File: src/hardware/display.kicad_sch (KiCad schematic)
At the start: 6 parts, among them J1 046809612110846+, U6 TXS0108ERKSR, U7 LP5817YCHR

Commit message: Add Light Sensor and Proximity & Gesture Sensor; Changed GPIO
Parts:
- renumbered R22 to R23
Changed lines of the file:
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@@
 		(dnp no)
 		(fields_autoplaced yes)
-		(property "Reference" "#PWR079"
+		(property "Reference" "#PWR080"
 			(at 90.17 130.81 0)
 			(effects
@@
 			(project "raywatch"
 				(path "/7b654ee8-2a53-4d39-8b7d-32c7bb3cb0ed/0522506d-d6b7-4115-aecc-a1b886294452"
-					(reference "#PWR079")
+					(reference "#PWR080")
 					(unit 1)
 				)
@@
 		(dnp no)
 		(fields_autoplaced yes)
-		(property "Reference" "#PWR094"
+		(property "Reference" "#PWR095"
 			(at 215.9 69.85 0)
 			(effects
@@
 			(project "raywatch"
 				(path "/7b654ee8-2a53-4d39-8b7d-32c7bb3cb0ed/0522506d-d6b7-4115-aecc-a1b886294452"
-					(reference "#PWR094")
+					(reference "#PWR095")
 					(unit 1)
 				)
@@
 		(dnp no)
 		(fields_autoplaced yes)
-		(property "Reference" "#PWR082"
+		(property "Reference" "#PWR083"
 			(at 110.49 40.64 0)
 			(effects
@@
 			(project "raywatch"
 				(path "/7b654ee8-2a53-4d39-8b7d-32c7bb3cb0ed/0522506d-d6b7-4115-aecc-a1b886294452"
-					(reference "#PWR082")
+					(reference "#PWR083")
 					(unit 1)
 				)
@@
 		(dnp no)
 		(fields_autoplaced yes)
-		(property "Reference" "R22"
+		(property "Reference" "R23"
 			(at 102.87 63.5 90)
 			(effects
@@
 			(project "raywatch"
 				(path "/7b654ee8-2a53-4d39-8b7d-32c7bb3cb0ed/0522506d-d6b7-4115-aecc-a1b886294452"
-					(reference "R22")
+					(reference "R23")
 					(unit 1)
 				)
@@
 		(dnp no)
 		(fields_autoplaced yes)
-		(property "Reference" "#PWR080"
+		(property "Reference" "#PWR081"
 			(at 90.17 140.97 0)
 			(effects
@@
 			(project "raywatch"
 				(path "/7b654ee8-2a53-4d39-8b7d-32c7bb3cb0ed/0522506d-d6b7-4115-aecc-a1b886294452"
-					(reference "#PWR080")
+					(reference "#PWR081")
 					(unit 1)
 				)
@@
 		(dnp no)
 		(fields_autoplaced yes)
-		(property "Reference" "#PWR087"
+		(property "Reference" "#PWR088"
 			(at 106.68 138.43 0)
 			(effects
@@
 			(project "raywatch"
 				(path "/7b654ee8-2a53-4d39-8b7d-32c7bb3cb0ed/0522506d-d6b7-4115-aecc-a1b886294452"
-					(reference "#PWR087")
+					(reference "#PWR088")
 					(unit 1)
 				)
@@
 		(dnp no)
 		(fields_autoplaced yes)
-		(property "Reference" "#PWR090"
+		(property "Reference" "#PWR091"
 			(at 176.53 87.63 0)
 			(effects
@@
 			(project "raywatch"
 				(path "/7b654ee8-2a53-4d39-8b7d-32c7bb3cb0ed/0522506d-d6b7-4115-aecc-a1b886294452"
-					(reference "#PWR090")
+					(reference "#PWR091")
 					(unit 1)
 				)
@@
 		(dnp no)
 		(fields_autoplaced yes)
-		(property "Reference" "#PWR088"
+		(property "Reference" "#PWR089"
 			(at 153.67 114.3 0)
 			(effects
@@
 			(project "raywatch"
 				(path "/7b654ee8-2a53-4d39-8b7d-32c7bb3cb0ed/0522506d-d6b7-4115-aecc-a1b886294452"
-					(reference "#PWR088")
+					(reference "#PWR089")
 					(unit 1)
 				)
@@
 		(dnp no)
 		(fields_autoplaced yes)
-		(property "Reference" "#PWR083"
+		(property "Reference" "#PWR084"
 			(at 110.49 43.18 0)
 			(effects
@@
 			(project "raywatch"
 				(path "/7b654ee8-2a53-4d39-8b7d-32c7bb3cb0ed/0522506d-d6b7-4115-aecc-a1b886294452"
-					(reference "#PWR083")
+					(reference "#PWR084")
 					(unit 1)
 				)
@@
 		(dnp no)
 		(fields_autoplaced yes)
-		(property "Reference" "#PWR084"
+		(property "Reference" "#PWR085"
 			(at 100.33 48.26 0)
 			(effects
@@
 			(project "raywatch"
 				(path "/7b654ee8-2a53-4d39-8b7d-32c7bb3cb0ed/0522506d-d6b7-4115-aecc-a1b886294452"
-					(reference "#PWR084")
+					(reference "#PWR085")
 					(unit 1)
 				)
@@
 		(dnp no)
 		(fields_autoplaced yes)
-		(property "Reference" "#PWR089"
+		(property "Reference" "#PWR090"
 			(at 165.1 93.98 0)
 			(effects
@@
 			(project "raywatch"
 				(path "/7b654ee8-2a53-4d39-8b7d-32c7bb3cb0ed/0522506d-d6b7-4115-aecc-a1b886294452"
-					(reference "#PWR089")
+					(reference "#PWR090")
 					(unit 1)
 				)
@@
 		(dnp no)
 		(fields_autoplaced yes)
-		(property "Reference" "#PWR081"
+		(property "Reference" "#PWR082"
 			(at 92.71 69.85 0)
 			(effects
@@
 			(project "raywatch"
 				(path "/7b654ee8-2a53-4d39-8b7d-32c7bb3cb0ed/0522506d-d6b7-4115-aecc-a1b886294452"
-					(reference "#PWR081")
+					(reference "#PWR082")
 					(unit 1)
 				)
@@
 		(dnp no)
 		(fields_autoplaced yes)
-		(property "Reference" "#PWR085"
+		(property "Reference" "#PWR086"
 			(at 100.33 50.8 0)
 			(effects
@@
 			(project "raywatch"
 				(path "/7b654ee8-2a53-4d39-8b7d-32c7bb3cb0ed/0522506d-d6b7-4115-aecc-a1b886294452"
-					(reference "#PWR085")
+					(reference "#PWR086")
 					(unit 1)
 				)
@@
 		(dnp no)
 		(fields_autoplaced yes)
-		(property "Reference" "#PWR091"
+		(property "Reference" "#PWR092"
 			(at 166.37 90.17 0)
 			(effects
@@
 			(project "raywatch"
 				(path "/7b654ee8-2a53-4d39-8b7d-32c7bb3cb0ed/0522506d-d6b7-4115-aecc-a1b886294452"
-					(reference "#PWR091")
+					(reference "#PWR092")
 					(unit 1)
 				)
@@
 		(dnp no)
 		(fields_autoplaced yes)
-		(property "Reference" "#PWR095"
+		(property "Reference" "#PWR096"
 			(at 215.9 72.39 0)
 			(effects
@@
 			(project "raywatch"
 				(path "/7b654ee8-2a53-4d39-8b7d-32c7bb3cb0ed/0522506d-d6b7-4115-aecc-a1b886294452"
-					(reference "#PWR095")
+					(reference "#PWR096")
 					(unit 1)
 				)
@@
 		(dnp no)
 		(fields_autoplaced yes)
-		(property "Reference" "#PWR086"
+		(property "Reference" "#PWR087"
 			(at 100.33 121.92 0)
 			(effects
@@
 			(project "raywatch"
 				(path "/7b654ee8-2a53-4d39-8b7d-32c7bb3cb0ed/0522506d-d6b7-4115-aecc-a1b886294452"
-					(reference "#PWR086")
+					(reference "#PWR087")
 					(unit 1)
 				)
@@
 		(dnp no)
 		(fields_autoplaced yes)
-		(property "Reference" "#PWR093"
+		(property "Reference" "#PWR094"
 			(at 173.99 63.5 0)
 			(effects
@@
 			(project "raywatch"
 				(path "/7b654ee8-2a53-4d39-8b7d-32c7bb3cb0ed/0522506d-d6b7-4115-aecc-a1b886294452"
-					(reference "#PWR093")
+					(reference "#PWR094")
 					(unit 1)
 				)
@@
 		(dnp no)
 		(fields_autoplaced yes)
-		(property "Reference" "#PWR092"
+		(property "Reference" "#PWR093"
 			(at 172.72 111.76 0)
 			(effects
@@
 			(project "raywatch"
 				(path "/7b654ee8-2a53-4d39-8b7d-32c7bb3cb0ed/0522506d-d6b7-4115-aecc-a1b886294452"
-					(reference "#PWR092")
-					(unit 1)
-				)
+					(reference "#PWR093")
+					(unit 1)
+				)

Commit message: Changed footprints from 0603 to 0402
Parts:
- C28, C29: footprint Capacitor_SMD:C_0603_1608Metric -> Capacitor_SMD:C_0504_1310Metric
- R23: footprint Resistor_SMD:R_0603_1608Metric -> Resistor_SMD:R_0402_1005Metric
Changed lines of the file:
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@@
 			)
 		)
-		(property "Footprint" "Resistor_SMD:R_0603_1608Metric"
+		(property "Footprint" "Resistor_SMD:R_0402_1005Metric"
 			(at 102.87 71.628 90)
 			(effects
@@
 			)
 		)
-		(property "Footprint" "Capacitor_SMD:C_0603_1608Metric"
+		(property "Footprint" "Capacitor_SMD:C_0504_1310Metric"
 			(at 173.6852 105.41 0)
 			(effects
@@
 			)
 		)
-		(property "Footprint" "Capacitor_SMD:C_0603_1608Metric"
+		(property "Footprint" "Capacitor_SMD:C_0504_1310Metric"
 			(at 91.1352 134.62 0)
 			(effects

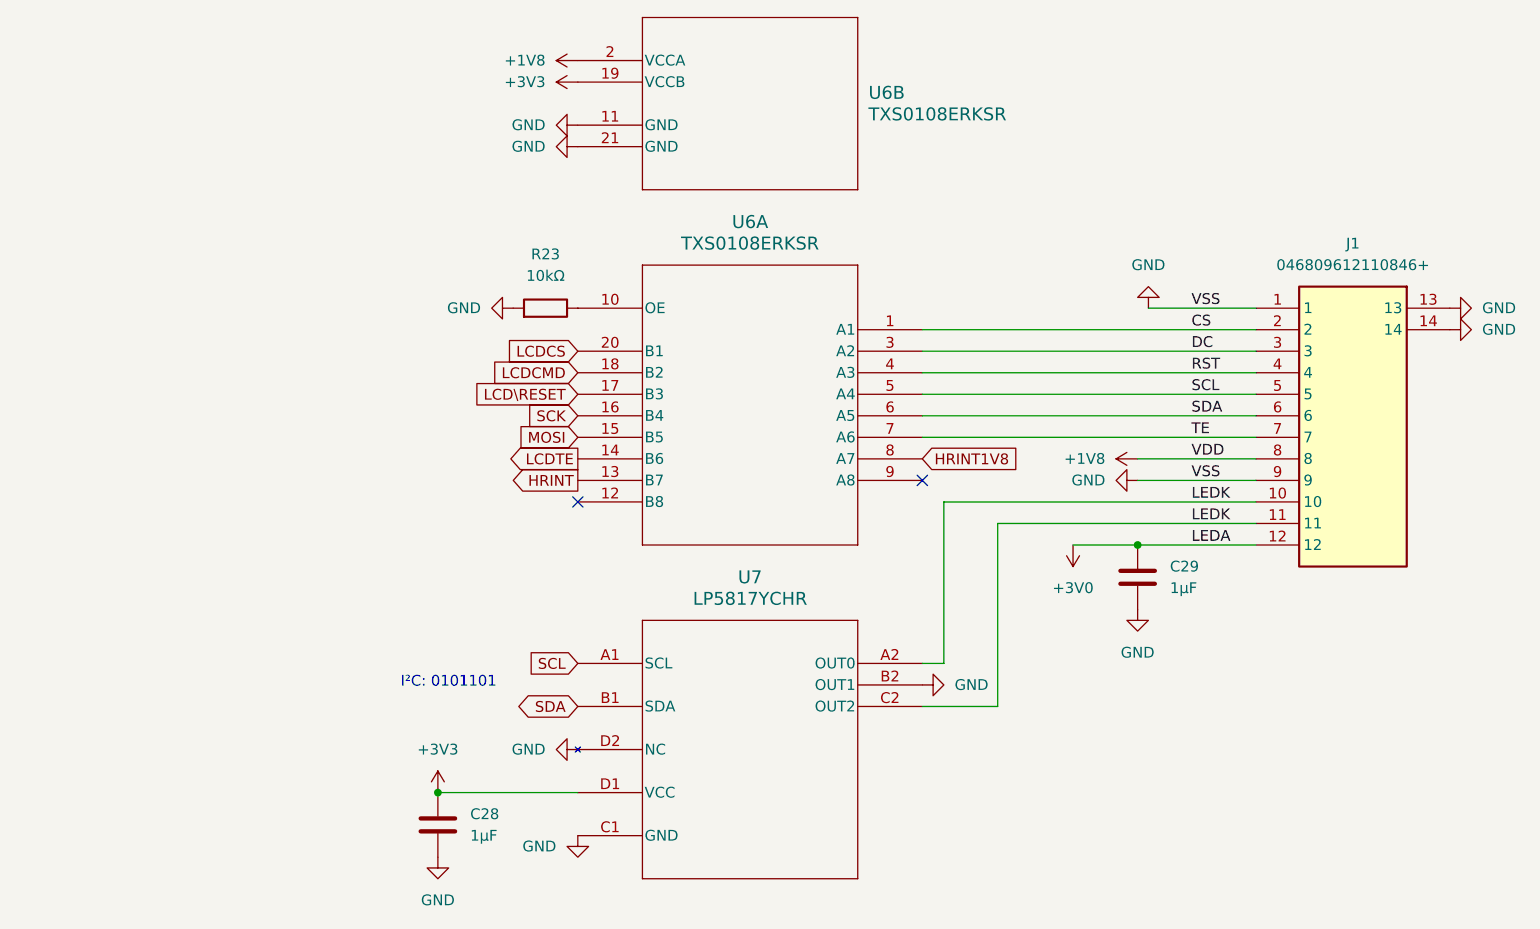
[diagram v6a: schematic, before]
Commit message: Replaced global labels with pin headers
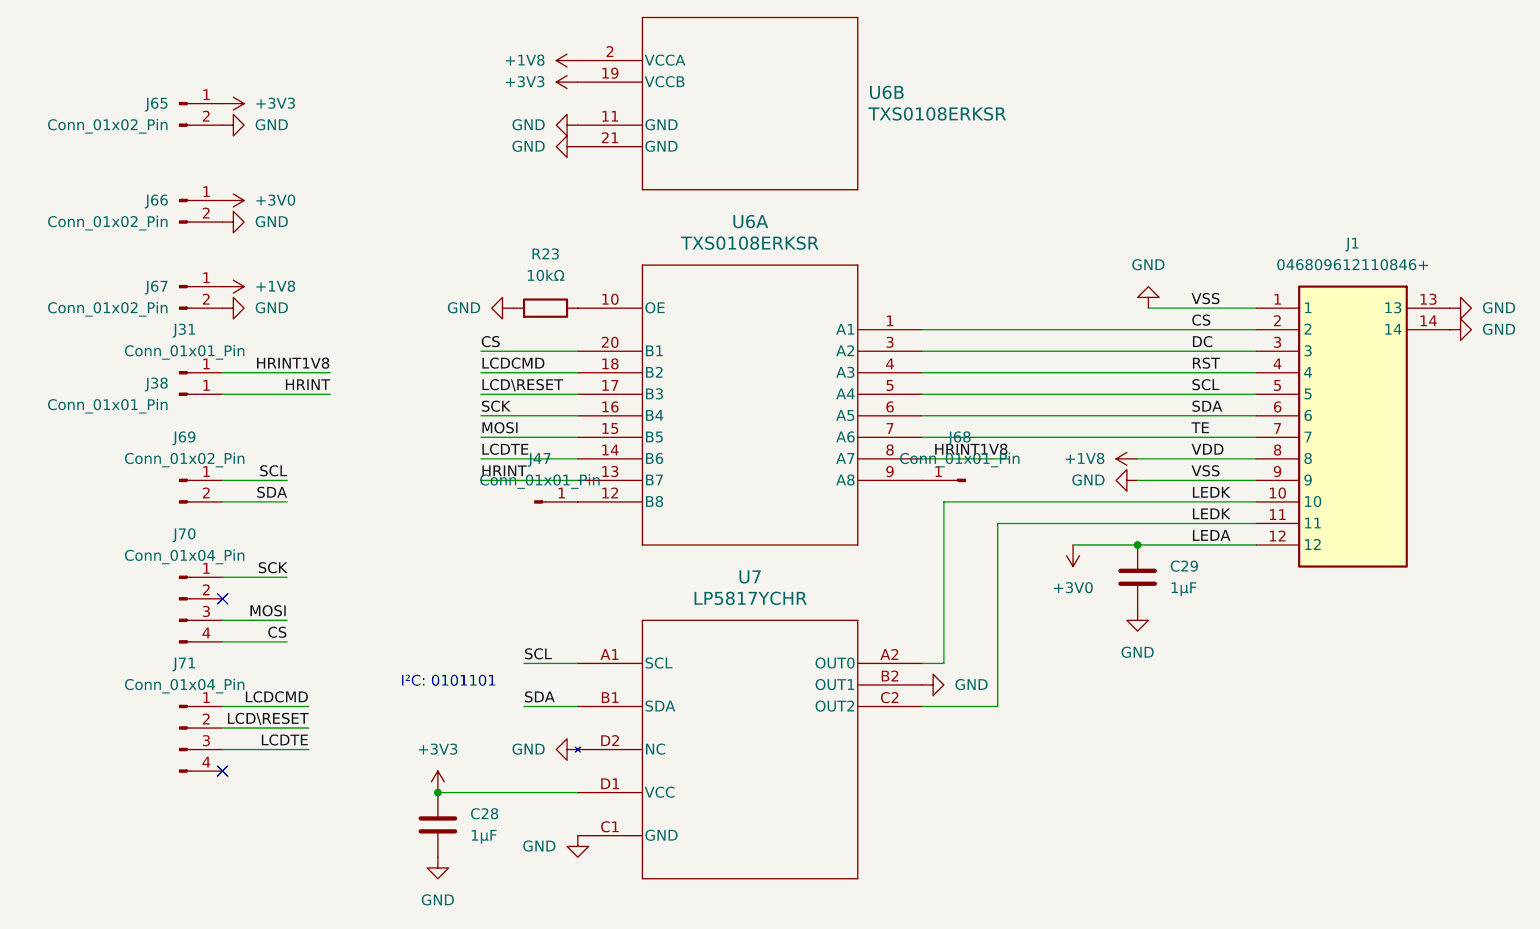
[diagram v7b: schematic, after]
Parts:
- added J31, J38, J47, J68: Conn_01x01_Pin, symbol Connector:Conn_01x01_Pin
- added J65, J66, J67, J69: Conn_01x02_Pin, symbol Connector:Conn_01x02_Pin
- added J70, J71: Conn_01x04_Pin, symbol Connector:Conn_01x04_Pin
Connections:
- net LCDCS is gone; now on net CS: U6.20 (B1)
- net +1V8: now also J67.1 (Pin_1)
- net +3V0: now also J66.1 (Pin_1)
- net +3V3: now also J65.1 (Pin_1)
- net CS: now also J70.4 (Pin_4)
- net GND: now also J65.2 (Pin_2), J66.2 (Pin_2), J67.2 (Pin_2)
- net HRINT: now also J38.1 (Pin_1)
- net HRINT1V8: now also J31.1 (Pin_1)
- net LCDCMD: now also J71.1 (Pin_1)
- net LCDTE: now also J71.3 (Pin_3)
- net LCD\RESET: now also J71.2 (Pin_2)
- net MOSI: now also J70.3 (Pin_3)
- net SCK: now also J70.1 (Pin_1)
- net SCL: now also J69.1 (Pin_1)
- net SDA: now also J69.2 (Pin_2)
- net at U6.12 (B8): now also J47.1 (Pin_1)
- net at U6.9 (A8): now also J68.1 (Pin_1)

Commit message: Reannotated schematic
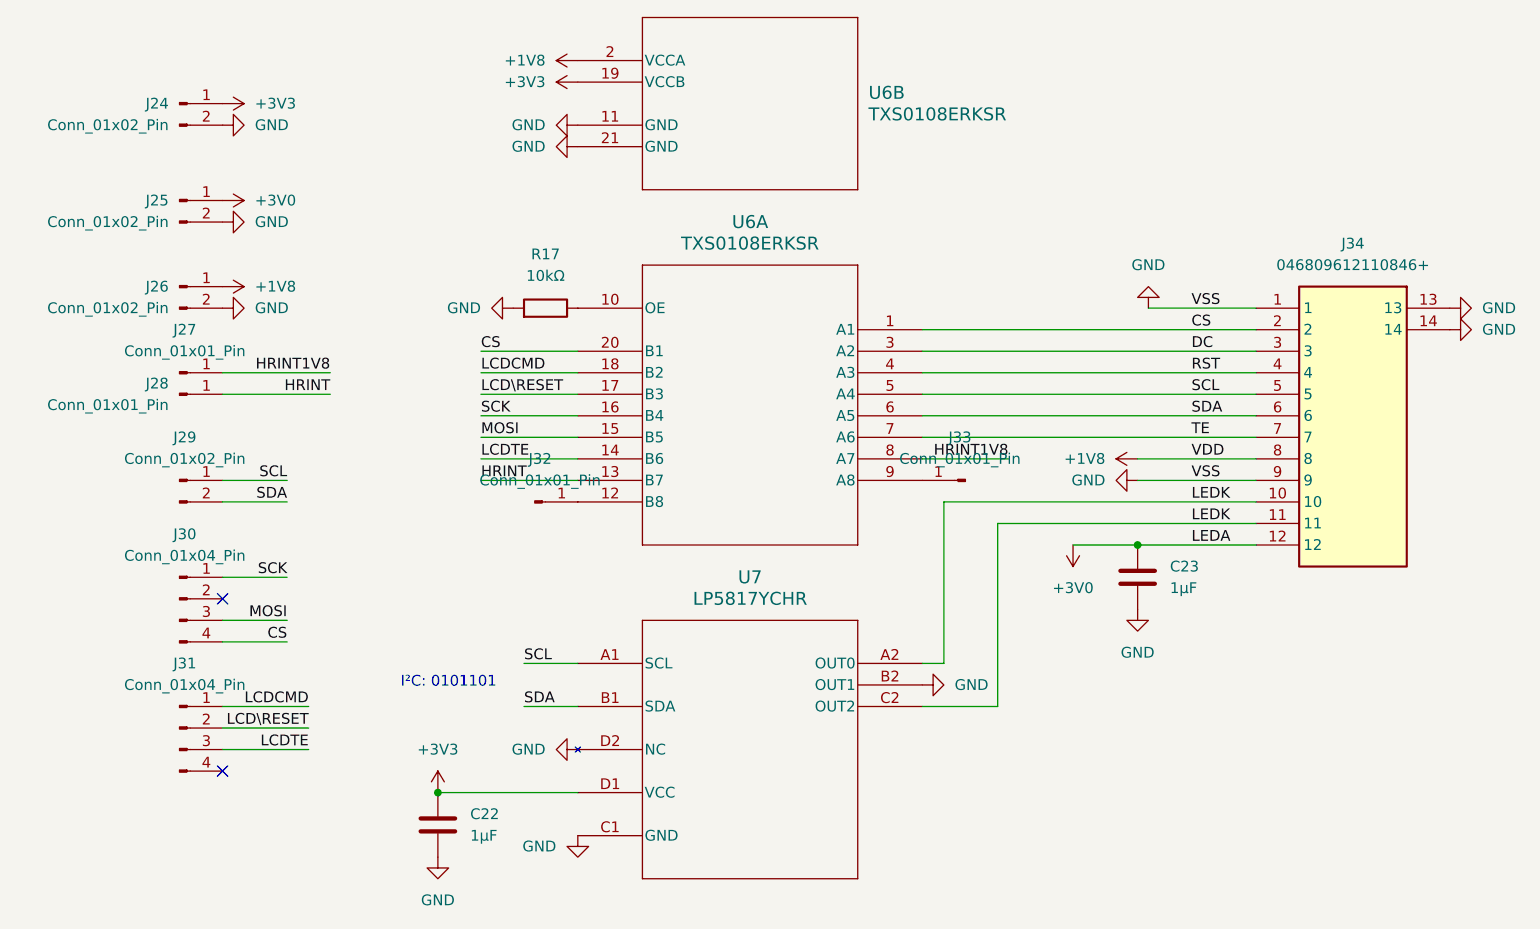
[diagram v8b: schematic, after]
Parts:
- renumbered C28 to C22, C29 to C23, J65 to J24, J66 to J25, J67 to J26, J31 to J27, J38 to J28, J69 to J29, J70 to J30, J71 to J31, J47 to J32, J68 to J33, J1 to J34, R23 to R17
